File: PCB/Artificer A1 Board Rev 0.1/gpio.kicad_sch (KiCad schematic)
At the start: 1 part, among them J1 Conn_02x20_Odd_Even

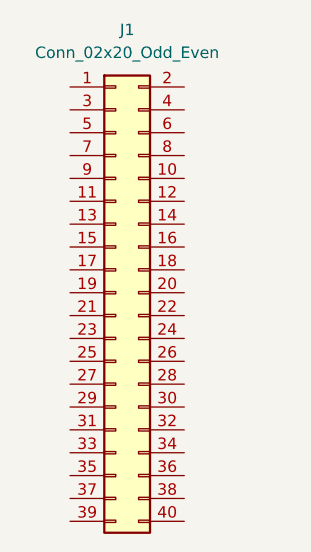
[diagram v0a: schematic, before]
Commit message: cleaned up, kicad 10 & usb c pd
migrated to Kicad 10,
added USB PD for power input
added capacitors inductors and resistor footprints
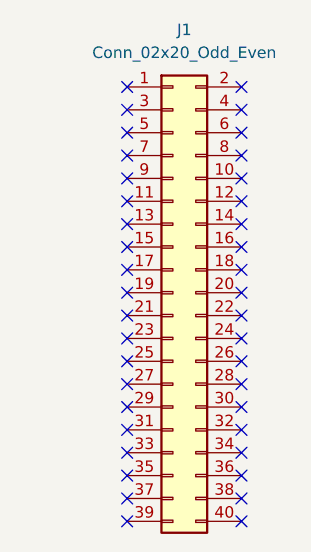
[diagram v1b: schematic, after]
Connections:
- no-connect marks 0 -> 40
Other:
- moved on the sheet: J1
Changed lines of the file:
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@@
 (kicad_sch
-	(version 20250114)
+	(version 20260306)
 	(generator "eeschema")
-	(generator_version "9.0")
+	(generator_version "10.0")
 	(paper "A4")
 	(title_block
@@
 		(company "Matthew Spotten")
 	)
+	(no_connect
+		(at 144.78 107.95)
+	)
+	(no_connect
+		(at 144.78 115.57)
+	)
+	(no_connect
+		(at 132.08 85.09)
+	)
+	(no_connect
+		(at 132.08 95.25)
+	)
+	(no_connect
+		(at 132.08 120.65)
+	)
+	(no_connect
+		(at 132.08 100.33)
+	)
+	(no_connect
+		(at 144.78 118.11)
+	)
+	(no_connect
+		(at 144.78 87.63)
+	)
+	(no_connect
+		(at 144.78 113.03)
+	)
+	(no_connect
+		(at 132.08 118.11)
+	)
+	(no_connect
+		(at 132.08 82.55)
+	)
+	(no_connect
+		(at 144.78 92.71)
+	)
+	(no_connect
+		(at 144.78 123.19)
+	)
+	(no_connect
+		(at 132.08 102.87)
+	)
+	(no_connect
+		(at 132.08 77.47)
+	)
+	(no_connect
+		(at 144.78 77.47)
+	)
+	(no_connect
+		(at 144.78 95.25)
+	)
+	(no_connect
+		(at 132.08 115.57)
+	)
+	(no_connect
+		(at 144.78 97.79)
+	)
+	(no_connect
+		(at 144.78 90.17)
+	)
+	(no_connect
+		(at 132.08 110.49)
+	)
+	(no_connect
+		(at 132.08 107.95)
+	)
+	(no_connect
+		(at 132.08 123.19)
+	)
+	(no_connect
+		(at 144.78 80.01)
+	)
+	(no_connect
+		(at 144.78 100.33)
+	)
+	(no_connect
+		(at 132.08 87.63)
+	)
+	(no_connect
+		(at 144.78 110.49)
+	)
+	(no_connect
+		(at 144.78 85.09)
+	)
+	(no_connect
+		(at 144.78 120.65)
+	)
+	(no_connect
+		(at 144.78 105.41)
+	)
+	(no_connect
+		(at 132.08 74.93)
+	)
+	(no_connect
+		(at 144.78 74.93)
+	)
+	(no_connect
+		(at 132.08 113.03)
+	)
+	(no_connect
+		(at 132.08 80.01)
+	)
+	(no_connect
+		(at 132.08 97.79)
+	)
+	(no_connect
+		(at 144.78 102.87)
+	)
+	(no_connect
+		(at 132.08 92.71)
+	)
+	(no_connect
+		(at 132.08 105.41)
+	)
+	(no_connect
+		(at 144.78 82.55)
+	)
+	(no_connect
+		(at 132.08 90.17)
+	)
 	(symbol
 		(lib_id "Connector_Generic:Conn_02x20_Odd_Even")
-		(at 130.81 97.79 0)
+		(at 137.16 97.79 0)
 		(unit 1)
+		(body_style 1)
 		(exclude_from_sim no)
 		(in_bom yes)
 		(on_board yes)
+		(in_pos_files yes)
 		(dnp no)
 		(fields_autoplaced yes)
 		(property "Reference" "J1"
-			(at 132.08 68.58 0)
+			(at 138.43 68.58 0)
+			(show_name no)
+			(do_not_autoplace no)
 			(effects
 				(font
@@
 		)
 		(property "Value" "Conn_02x20_Odd_Even"
-			(at 132.08 71.12 0)
+			(at 138.43 71.12 0)
+			(show_name no)
+			(do_not_autoplace no)
 			(effects
 				(font
@@
 		)
 		(property "Footprint" "Connector_PinHeader_2.54mm:PinHeader_2x20_P2.54mm_Vertical"
-			(at 130.81 97.79 0)
-			(effects
-				(font
-					(size 1.27 1.27)
-				)
-				(hide yes)
-			)
-		)
-		(property "Datasheet" "~"
-			(at 130.81 97.79 0)
-			(effects
-				(font
-					(size 1.27 1.27)
-				)
-				(hide yes)
+			(at 137.16 97.79 0)
+			(hide yes)
+			(show_name no)
+			(do_not_autoplace no)
+			(effects
+				(font
+					(size 1.27 1.27)
+				)
+			)
+		)
+		(property "Datasheet" ""
+			(at 137.16 97.79 0)
+			(hide yes)
+			(show_name no)
+			(do_not_autoplace no)
+			(effects
+				(font
+					(size 1.27 1.27)
+				)
 			)
 		)
 		(property "Description" "Generic connector, double row, 02x20, odd/even pin numbering scheme (row 1 odd numbers, row 2 even numbers), script generated (kicad-library-utils/schlib/autogen/connector/)"
-			(at 130.81 97.79 0)
-			(effects
-				(font
-					(size 1.27 1.27)
-				)
-				(hide yes)
+			(at 137.16 97.79 0)
+			(hide yes)
+			(show_name no)
+			(do_not_autoplace no)
+			(effects
+				(font
+					(size 1.27 1.27)
+				)
 			)
 		)
@@
 		)
 		(instances
-			(project ""
+			(project "Artificer A1 Board Rev 0.1"
 				(path "/7c37bdb5-94b0-4567-b5ec-a879db855389/25f75405-4979-49de-8ac1-70a85763767f"
 					(reference "J1")

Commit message: more routing and decoupling
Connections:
- net VCC-3V3: now reaches J1.1 (Pin_1)
- net VCC-3V3: now also J1.17 (Pin_17)
- net PL3: now reaches J1.10 (Pin_10)
- net PL4: now reaches J1.11 (Pin_11)
- net PL10: now reaches J1.12 (Pin_12)
- net PL5: now reaches J1.13 (Pin_13)
- net GND: now reaches J1.14 (Pin_14)
- net GND: now also J1.20 (Pin_20), J1.25 (Pin_25), J1.30 (Pin_30), J1.34 (Pin_34), J1.39 (Pin_39), J1.6 (Pin_6), J1.9 (Pin_9)
- net PL6: now reaches J1.15 (Pin_15)
- net PL7: now reaches J1.16 (Pin_16)
- net PI0: now reaches J1.18 (Pin_18)
- net PI4: now reaches J1.19 (Pin_19)
- net 5V_SYS: now reaches J1.2 (Pin_2)
- net 5V_SYS: now also J1.4 (Pin_4)
- net PI5: now reaches J1.21 (Pin_21)
- net PI1: now reaches J1.22 (Pin_22)
- net PI3: now reaches J1.23 (Pin_23)
- net PI2: now reaches J1.24 (Pin_24)
- net PI6: now reaches J1.26 (Pin_26)
- net PL9: now reaches J1.27 (Pin_27)
- net PL8: now reaches J1.28 (Pin_28)
- net PI9: now reaches J1.29 (Pin_29)
- net PL13: now reaches J1.3 (Pin_3)
- net PI10: now reaches J1.31 (Pin_31)
- net PI14: now reaches J1.32 (Pin_32)
- net PI11: now reaches J1.33 (Pin_33)
- net PI12: now reaches J1.35 (Pin_35)
- net PI15: now reaches J1.36 (Pin_36)
- net PI13: now reaches J1.37 (Pin_37)
- net PI8: now reaches J1.38 (Pin_38)
- net PI7: now reaches J1.40 (Pin_40)
- net PL12: now reaches J1.5 (Pin_5)
- net PL11: now reaches J1.7 (Pin_7)
- net PL2: now reaches J1.8 (Pin_8)
- no-connect marks 40 -> 0
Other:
- note added: "GPIO14 GPIO15 GPIO18 GPIO23 GPIO24 GPIO25 GPIO8 GPIO7 GPIO1 GPIO12 GPIO16 GPIO20 GPIO21"
- note added: "GPIO2 GPIO3 GPIO4 GPIO17 GPIO27 GPIO22 GPIO10 GPIO9 GPIO11 GPIO0 GPIO5 GPIO6 GPIO13 GPIO19 GPIO26"
- note added: "S-PWM0-0"
- note added: "S-TWI1-SCK"
- note added: "S-TWI1-SDA"
- note added: "S-UART0-RX"
- note added: "S-UART0-TX"
- note added: "SPI1_CE0"
- note added: "SPI1_MISO"
- note added: "SPI1_MOSI"
- note added: "SPI1_SCLK"
- note added: "SPI2_CE0"
- note added: "SPI2_MISO"
- note added: "SPI2_MOSI"
- note added: "SPI2_SCLK"
